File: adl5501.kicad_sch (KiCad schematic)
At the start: 7 parts, among them U1801 ADL5501AKSZ-R7

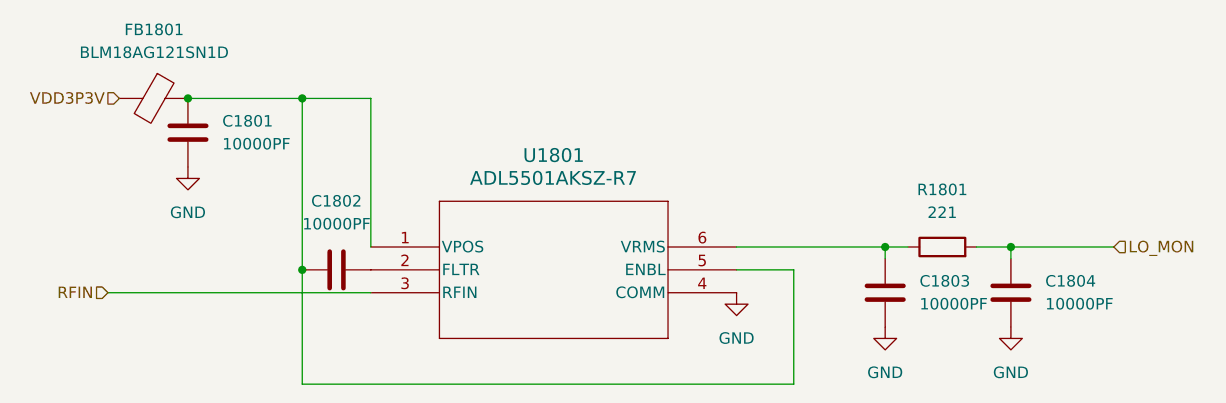
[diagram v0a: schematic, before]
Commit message: Updates from Michal to fix ERC errors
Still lots of ERC warnings
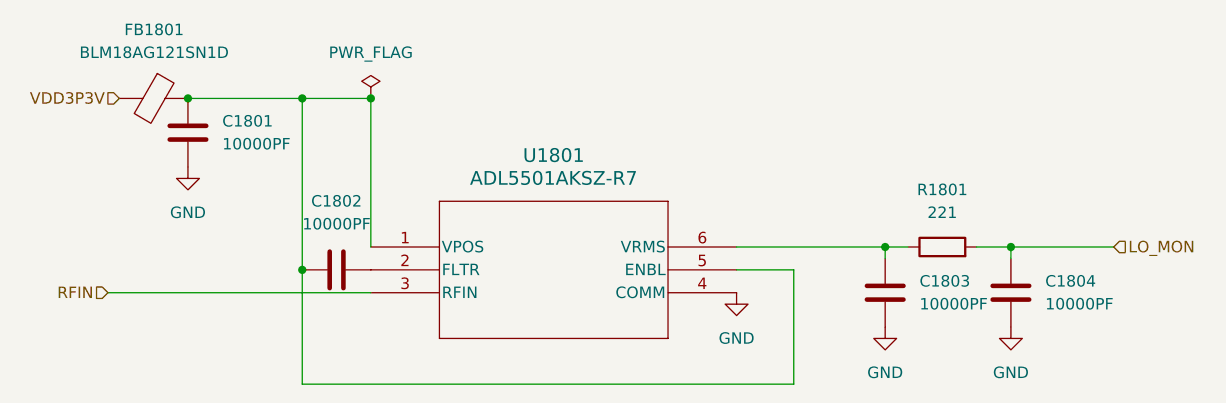
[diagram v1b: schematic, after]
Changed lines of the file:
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@@
+	)
+	(junction
+		(at 120.65 62.23)
+		(diameter 0)
+		(color 0 0 0 0)
 	)
 	(junction
@@
 					(unit 1)
 				)
+			)
+		)
+	)
+	(symbol
+		(lib_id "power:PWR_FLAG")
+		(at 120.65 62.23 0)
+		(unit 1)
+		(exclude_from_sim no)
+		(in_bom yes)
+		(on_board yes)
+		(dnp no)
+		(fields_autoplaced yes)
+		(property "Reference" "#FLG010"
+			(at 120.65 60.325 0)
+			(effects
+				(font
+					(size 1.27 1.27)
+				)
+				(hide yes)
+			)
+		)
+		(property "Value" "PWR_FLAG"
+			(at 120.65 57.15 0)
+			(effects
+				(font
+					(size 1.27 1.27)
+				)
+			)
+		)
+		(property "Footprint" ""
+			(at 120.65 62.23 0)
+			(effects
+				(font
+					(size 1.27 1.27)
+				)
+				(hide yes)
+			)
+		)
+		(property "Datasheet" "~"
+			(at 120.65 62.23 0)
+			(effects
+				(font
+					(size 1.27 1.27)
+				)
+				(hide yes)
+			)
+		)
+		(property "Description" "Special symbol for telling ERC where power comes from"
+			(at 120.65 62.23 0)
+			(effects
+				(font
+					(size 1.27 1.27)
+				)
+				(hide yes)
+			)
+		)
+		(pin "1"
+		)
+		(instances
+			(project "zest"
+				(path "/00000000-0000-0000-0000-000000000003/00000000-0000-0000-0000-00000000000c"
+					(reference "#FLG010")
+					(unit 1)
+				)

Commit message: Schematic Changes
Added Manufacturer/MPN/Description Fields to parts
Added libraries to project
Modified FMC schematic to use new symbol
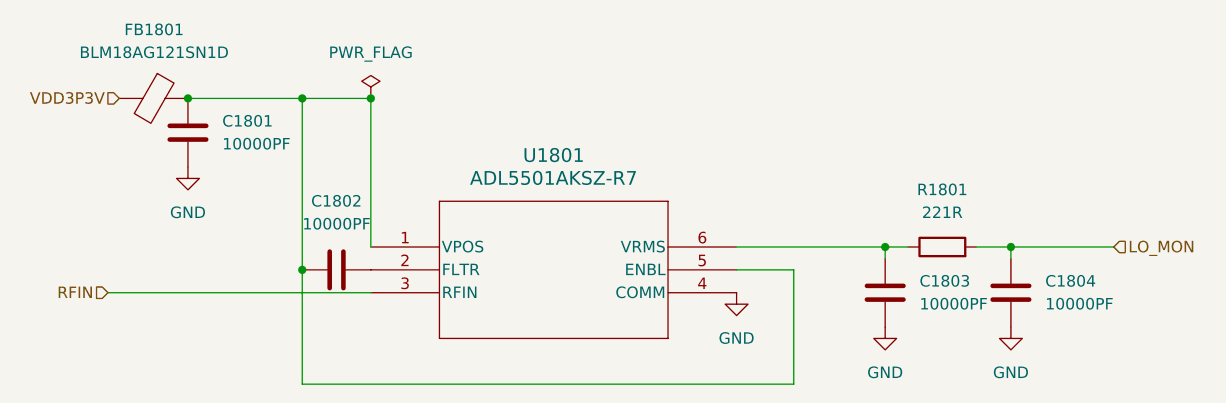
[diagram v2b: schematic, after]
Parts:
- C1801, C1802, C1803, C1804: Manufacturer (none) -> TDK; Manufacturer Part Number (none) -> C1608C0G1E103J080AA
- FB1801: Manufacturer (none) -> Murata; Manufacturer Part Number (none) -> BLM18AG121SN1D
- R1801: value 221 -> 221R; Manufacturer (none) -> YAGEO; Manufacturer Part Number (none) -> RC0603FR-07221RL
- U1801: Manufacturer (none) -> Analog Devices; Manufacturer Part Number (none) -> ADL5501AKSZ-R7
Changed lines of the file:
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@@
 			)
 		)
-		(property "Description" "Unpolarized capacitor"
+		(property "Description" "CAP CER 10000PF 25V C0G 0603"
 			(at 191.77 83.82 0)
 			(effects
@@
 			)
 		)
+		(property "Manufacturer" "TDK"
+			(at 191.77 83.82 0)
+			(effects
+				(font
+					(size 1.27 1.27)
+				)
+				(hide yes)
+			)
+		)
+		(property "Manufacturer Part Number" "C1608C0G1E103J080AA"
+			(at 191.77 83.82 0)
+			(effects
+				(font
+					(size 1.27 1.27)
+				)
+				(hide yes)
+			)
+		)
 		(pin "2"
 		)
@@
 			)
 		)
-		(property "Description" "Unpolarized capacitor"
+		(property "Description" "CAP CER 10000PF 25V C0G 0603"
 			(at 177.8 83.82 0)
 			(effects
@@
 			)
 		)
+		(property "Manufacturer" "TDK"
+			(at 177.8 83.82 0)
+			(effects
+				(font
+					(size 1.27 1.27)
+				)
+				(hide yes)
+			)
+		)
+		(property "Manufacturer Part Number" "C1608C0G1E103J080AA"
+			(at 177.8 83.82 0)
+			(effects
+				(font
+					(size 1.27 1.27)
+				)
+				(hide yes)
+			)
+		)
 		(pin "2"
 		)
@@
 			)
 		)
-		(property "Description" "Unpolarized capacitor"
+		(property "Description" "CAP CER 10000PF 25V C0G 0603"
 			(at 100.33 66.04 0)
 			(effects
@@
 			)
 		)
+		(property "Manufacturer" "TDK"
+			(at 100.33 66.04 0)
+			(effects
+				(font
+					(size 1.27 1.27)
+				)
+				(hide yes)
+			)
+		)
+		(property "Manufacturer Part Number" "C1608C0G1E103J080AA"
+			(at 100.33 66.04 0)
+			(effects
+				(font
+					(size 1.27 1.27)
+				)
+				(hide yes)
+			)
+		)
 		(pin "1"
 		)
@@
 			)
 		)
-		(property "Value" "221"
+		(property "Value" "221R"
 			(at 184.15 74.93 90)
 			(effects
@@
 			)
 		)
-		(property "Description" "Resistor"
+		(property "Description" "RES 221 OHM 1% 1/10W 0603"
 			(at 184.15 78.74 0)
 			(effects
@@
 			)
 		)
+		(property "Manufacturer" "YAGEO "
+			(at 184.15 78.74 0)
+			(effects
+				(font
+					(size 1.27 1.27)
+				)
+				(hide yes)
+			)
+		)
+		(property "Manufacturer Part Number" "RC0603FR-07221RL "
+			(at 184.15 78.74 0)
+			(effects
+				(font
+					(size 1.27 1.27)
+				)
+				(hide yes)
+			)
+		)
 		(pin "1"
 		)
@@
 			)
 		)
-		(property "Description" "Ferrite bead"
+		(property "Description" "FERRITE BEAD 120 OHM 0603 1LN"
 			(at 96.52 62.23 0)
 			(effects
@@
 			)
 		)
+		(property "Manufacturer" "Murata"
+			(at 96.52 62.23 0)
+			(effects
+				(font
+					(size 1.27 1.27)
+				)
+				(hide yes)
+			)
+		)
+		(property "Manufacturer Part Number" "BLM18AG121SN1D "
+			(at 96.52 62.23 0)
+			(effects
+				(font
+					(size 1.27 1.27)
+				)
+				(hide yes)
+			)
+		)
 		(pin "2"
 		)
@@
 			)
 		)
-		(property "Description" ""
+		(property "Description" "IC RF DETECT 50MHZ-6GHZ SC70-6"
 			(at 120.65 78.74 0)
 			(effects
@@
 			)
 		)
+		(property "Manufacturer" "Analog Devices"
+			(at 120.65 78.74 0)
+			(effects
+				(font
+					(size 1.27 1.27)
+				)
+				(hide yes)
+			)
+		)
+		(property "Manufacturer Part Number" "ADL5501AKSZ-R7 "
+			(at 120.65 78.74 0)
+			(effects
+				(font
+					(size 1.27 1.27)
+				)
+				(hide yes)
+			)
+		)
 		(pin "5"
 		)
@@
 			)
 		)
-		(property "Description" "Unpolarized capacitor"
+		(property "Description" "CAP CER 10000PF 25V C0G 0603"
 			(at 116.84 81.28 0)
 			(effects
@@
 			(effects
 				(font
+					(size 1.27 1.27)
+				)
+				(hide yes)
+			)
+		)
+		(property "Manufacturer" "TDK"
+			(at 116.84 81.28 0)
+			(effects
+				(font
+					(size 1.27 1.27)
+				)
+				(hide yes)
+			)
+		)
+		(property "Manufacturer Part Number" "C1608C0G1E103J080AA"
+			(at 116.84 81.28 0)
+			(effects
+				(font

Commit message: Schematics update
Cleaned up RF ADC and front end sections.
Verified that changes did not changes anything about the layout.
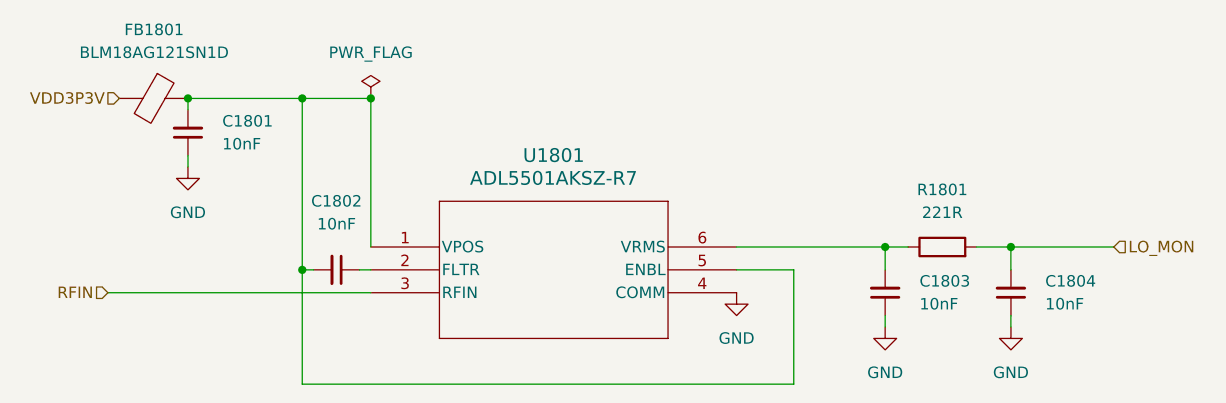
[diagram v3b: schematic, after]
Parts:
- C1801, C1802, C1803, C1804: value 10000PF -> 10nF; symbol Device:C -> Device:C_Small
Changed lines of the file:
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@@
 	(paper "A4")
+	(junction
+		(at 113.03 81.28)
+		(diameter 0)
+		(color 0 0 0 0)
+	)
 	(junction
 		(at 100.33 62.23)
@@
 	)
 	(junction
-		(at 113.03 81.28)
-		(diameter 0)
-		(color 0 0 0 0)
-	)
-	(junction
 		(at 113.03 62.23)
 		(diameter 0)
@@
 	(wire
 		(pts
-			(xy 177.8 78.74) (xy 177.8 80.01)
+			(xy 177.8 78.74) (xy 177.8 81.28)
+		)
+		(stroke
+			(width 0)
+			(type default)
+		)
+	)
+	(wire
+		(pts
+			(xy 100.33 68.58) (xy 100.33 69.85)
+		)
+		(stroke
+			(width 0)
+			(type default)
+		)
+	)
+	(wire
+		(pts
+			(xy 177.8 86.36) (xy 177.8 87.63)
 		)
 		(stroke
@@
 	(wire
 		(pts
+			(xy 113.03 62.23) (xy 113.03 81.28)
+		)
+		(stroke
+			(width 0)
+			(type default)
+		)
+	)
+	(wire
+		(pts
 			(xy 120.65 62.23) (xy 113.03 62.23)
 		)
@@
 	(wire
 		(pts
+			(xy 191.77 86.36) (xy 191.77 87.63)
+		)
+		(stroke
+			(width 0)
+			(type default)
+		)
+	)
+	(wire
+		(pts
 			(xy 167.64 93.98) (xy 167.64 81.28)
 		)
@@
 	(wire
 		(pts
+			(xy 100.33 62.23) (xy 100.33 63.5)
+		)
+		(stroke
+			(width 0)
+			(type default)
+		)
+	)
+	(wire
+		(pts
 			(xy 100.33 62.23) (xy 113.03 62.23)
 		)
@@
 	(wire
 		(pts
-			(xy 113.03 62.23) (xy 113.03 81.28)
-		)
-		(stroke
-			(width 0)
-			(type default)
-		)
-	)
-	(wire
-		(pts
-			(xy 191.77 78.74) (xy 191.77 80.01)
+			(xy 113.03 81.28) (xy 114.3 81.28)
+		)
+		(stroke
+			(width 0)
+			(type default)
+		)
+	)
+	(wire
+		(pts
+			(xy 191.77 78.74) (xy 191.77 81.28)
+		)
+		(stroke
+			(width 0)
+			(type default)
+		)
+	)
+	(wire
+		(pts
+			(xy 119.38 81.28) (xy 120.65 81.28)
 		)
 		(stroke
@@
 	)
 	(symbol
-		(lib_id "Device:C")
+		(lib_id "Device:C_Small")
 		(at 191.77 83.82 180)
 		(unit 1)
@@
 			)
 		)
-		(property "Value" "10000PF"
+		(property "Value" "10nF"
 			(at 195.58 85.0899 0)
 			(effects
@@
 			)
 		)
-		(property "Description" "CAP CER 10000PF 25V C0G 0603"
+		(property "Description" "CAP CER 10nF 25V C0G 0603"
 			(at 191.77 83.82 0)
 			(effects
@@
 	)
 	(symbol
-		(lib_id "Device:C")
+		(lib_id "Device:C_Small")
 		(at 177.8 83.82 180)
 		(unit 1)
@@
 			)
 		)
-		(property "Value" "10000PF"
+		(property "Value" "10nF"
 			(at 181.61 85.0899 0)
 			(effects
@@
 			)
 		)
-		(property "Description" "CAP CER 10000PF 25V C0G 0603"
+		(property "Description" "CAP CER 10nF 25V C0G 0603"
 			(at 177.8 83.82 0)
 			(effects
@@
 	)
 	(symbol
-		(lib_id "Device:C")
+		(lib_id "Device:C_Small")
 		(at 100.33 66.04 180)
 		(unit 1)
@@
 			)
 		)
-		(property "Value" "10000PF"
+		(property "Value" "10nF"
 			(at 104.14 67.3099 0)
 			(effects
@@
 			)
 		)
-		(property "Description" "CAP CER 10000PF 25V C0G 0603"
+		(property "Description" "CAP CER 10nF 25V C0G 0603"
 			(at 100.33 66.04 0)
 			(effects
@@
 	)
 	(symbol
-		(lib_id "Device:C")
+		(lib_id "Device:C_Small")
 		(at 116.84 81.28 270)
 		(unit 1)
@@
 			)
 		)
-		(property "Value" "10000PF"
+		(property "Value" "10nF"
 			(at 116.84 76.2 90)
 			(effects
@@
 			)
 		)
-		(property "Description" "CAP CER 10000PF 25V C0G 0603"
+		(property "Description" "CAP CER 10nF 25V C0G 0603"
 			(at 116.84 81.28 0)
 			(effects
